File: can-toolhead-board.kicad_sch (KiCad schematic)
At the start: 40 parts, among them J1 MF3-2x2P, J2 USB_C_Receptacle_USB2.0, J3 SH-6P, SW1 SW_Push, SW2 SW_Push, U1 TPS62933, U2 MIC5365-3.3YC5, U3 TJA1051TK-3, U4 STM32G0B1KBU6, U7 USBLC6-2P6

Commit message: Add part number references
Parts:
- C1: MPN EEH-ZK1V101XP -> (none); manf# (none) -> GYE1V101MCQ1GS
- C10, C11, C12, C3, C4, C5: manf# (none) -> GRM155R71H104KE14J
- C2: manf# (none) -> GRM21BR61H106KE43L
- C6: manf# (none) -> CL05C470JB5NNNC
- C7: manf# (none) -> CL10A226MP8NUNE
- C8: manf# (none) -> CL10A475KO8NNNC
- C9: manf# (none) -> CL05B103KB5NNNC
- D1: MPN SS34 -> (none); digikey# (none) -> 641-2115-1-ND; manf# (none) -> SS34
- D2: MPN DSS14 -> (none); digikey# (none) -> 1655-DSS14UCT-ND; manf# (none) -> DSS14
- D6: manf# (none) -> LTST-S270KGKT
- H1, H2, JP1, JP5, JP6: now left out of the parts list
- J1: MPN 43045-0400 -> (none); manf# (none) -> 43045-0400
- J2: MPN TYPE-C-31-M-12 -> (none); manf# (none) -> 12402012E212A
- J3: manf# (none) -> SM06B-SRSS-TB
- JP2: manf# (none) -> M22-2010205
- L1: MPN IHLP2020CZER3R3M11 -> (none); manf# (none) -> IHLP2020CZER3R3M11
- R1: manf# (none) -> RMCF0402JT120R
- R2: value 52K3 -> 52K3 1%; manf# (none) -> RMCF0402FT52K3
- R3: value 10K -> 10K 1%; manf# (none) -> RMCF0402FT10K0
- R31, R7: manf# (none) -> RMCF0402FT10K0
- R4: manf# (none) -> RMCF0402JT100K
- R5, R6: manf# (none) -> RMCF0402JT5K10
- SW1, SW2: MPN KMR211GLFS -> (none); manf# (none) -> EVQ-P7A01P
- U1: MPN TPS62933DRLR -> (none); manf# (none) -> TPS62933DRLR
- U2: MPN TLV70033DCKR -> (none); manf# (none) -> TLV70033DCKR
- U3: manf# (none) -> TJA1051TK/3/1J
- U4: MPN STM32G0B1KBU6 -> (none); manf# (none) -> STM32G0B1KBU6
- U7: MPN USBLC6-2P6 -> (none); manf# (none) -> USBLC6-2P6
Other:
- moved on the sheet: C7

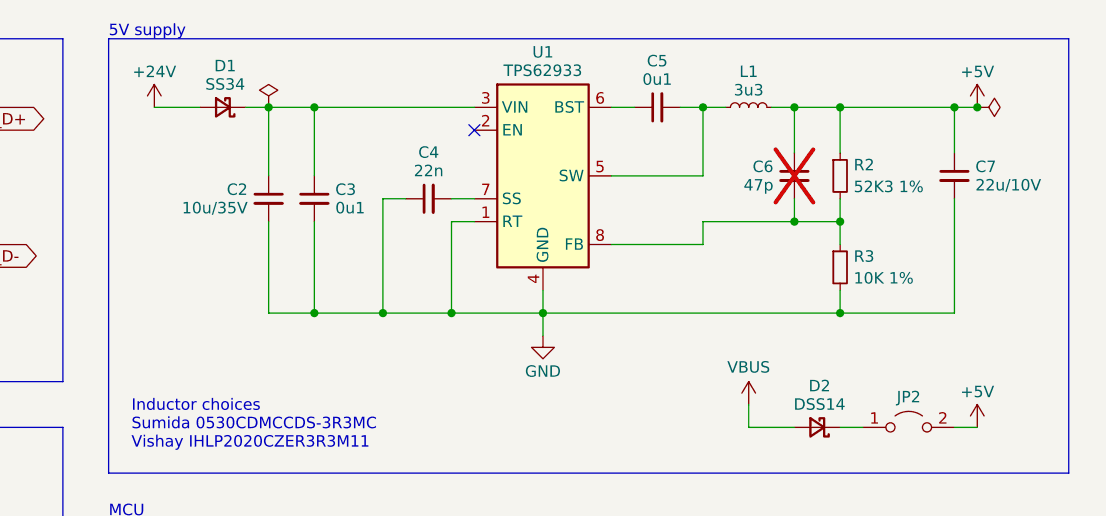
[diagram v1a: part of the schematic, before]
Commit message: Change input caps
- 100uF to electrolytic
- 10uF to 1206/50V
- Also fix LED on BOM to not be right angle lol
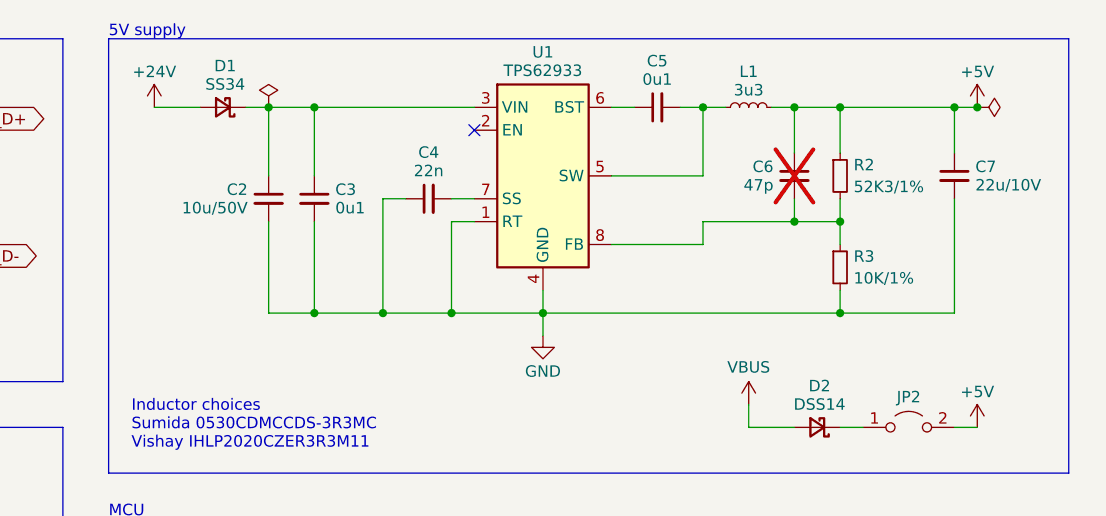
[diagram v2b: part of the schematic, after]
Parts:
- C1: LCSC C454360 -> C705528; manf# GYE1V101MCQ1GS -> EEE-TQV101XAP
- C2: value 10u/35V -> 10u/50V; footprint Capacitor_SMD:C_0805_2012Metric -> Capacitor_SMD:C_1206_3216Metric; LCSC C440198 -> C2987934; manf# GRM21BR61H106KE43L -> GRM31CD71H106KE11
- D6: manf# LTST-S270KGKT -> LTST-C190KGKT
- R2: value 52K3 1% -> 52K3/1%
- R3: value 10K 1% -> 10K/1%
- SW1, SW2: LCSC C221675 -> C79167
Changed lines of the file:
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@@
 			)
 		)
-		(property "Value" "10u/35V"
+		(property "Value" "10u/50V"
 			(at 117.056 41.6703 0)
 			(effects
@@
 			)
 		)
-		(property "Footprint" "Capacitor_SMD:C_0805_2012Metric"
+		(property "Footprint" "Capacitor_SMD:C_1206_3216Metric"
 			(at 119.38 40.64 0)
 			(effects
@@
 			)
 		)
-		(property "manf#" "GRM21BR61H106KE43L"
+		(property "manf#" "GRM31CD71H106KE11 "
 			(at 119.38 40.64 0)
 			(effects
@@
 			)
 		)
-		(property "LCSC" "C440198"
+		(property "LCSC" "C2987934"
 			(at 119.38 40.64 0)
 			(effects
@@
 			)
 		)
-		(property "LCSC" "C221675"
+		(property "LCSC" "C79167"
 			(at 213.36 139.7 0)
 			(effects
@@
 			)
 		)
-		(property "manf#" "LTST-S270KGKT"
+		(property "manf#" "LTST-C190KGKT"
 			(at 261.62 38.1 0)
 			(effects
@@
 			)
 		)
-		(property "LCSC" "C454360"
+		(property "LCSC" "C705528"
 			(at 38.1 39.37 0)
 			(effects
@@
 			)
 		)
-		(property "manf#" "GYE1V101MCQ1GS"
+		(property "manf#" "EEE-TQV101XAP"
 			(at 38.1 39.37 0)
 			(effects
@@
 			)
 		)
-		(property "LCSC" "C221675"
+		(property "LCSC" "C79167"
 			(at 111.76 104.14 0)
 			(effects
@@
 			)
 		)
-		(property "Value" "10K 1%"
+		(property "Value" "10K/1%"
 			(at 184.3786 49.4721 0)
 			(effects
@@
 			)
 		)
-		(property "Value" "52K3 1%"
+		(property "Value" "52K3/1%"
 			(at 184.3786 39.3121 0)
 			(effects

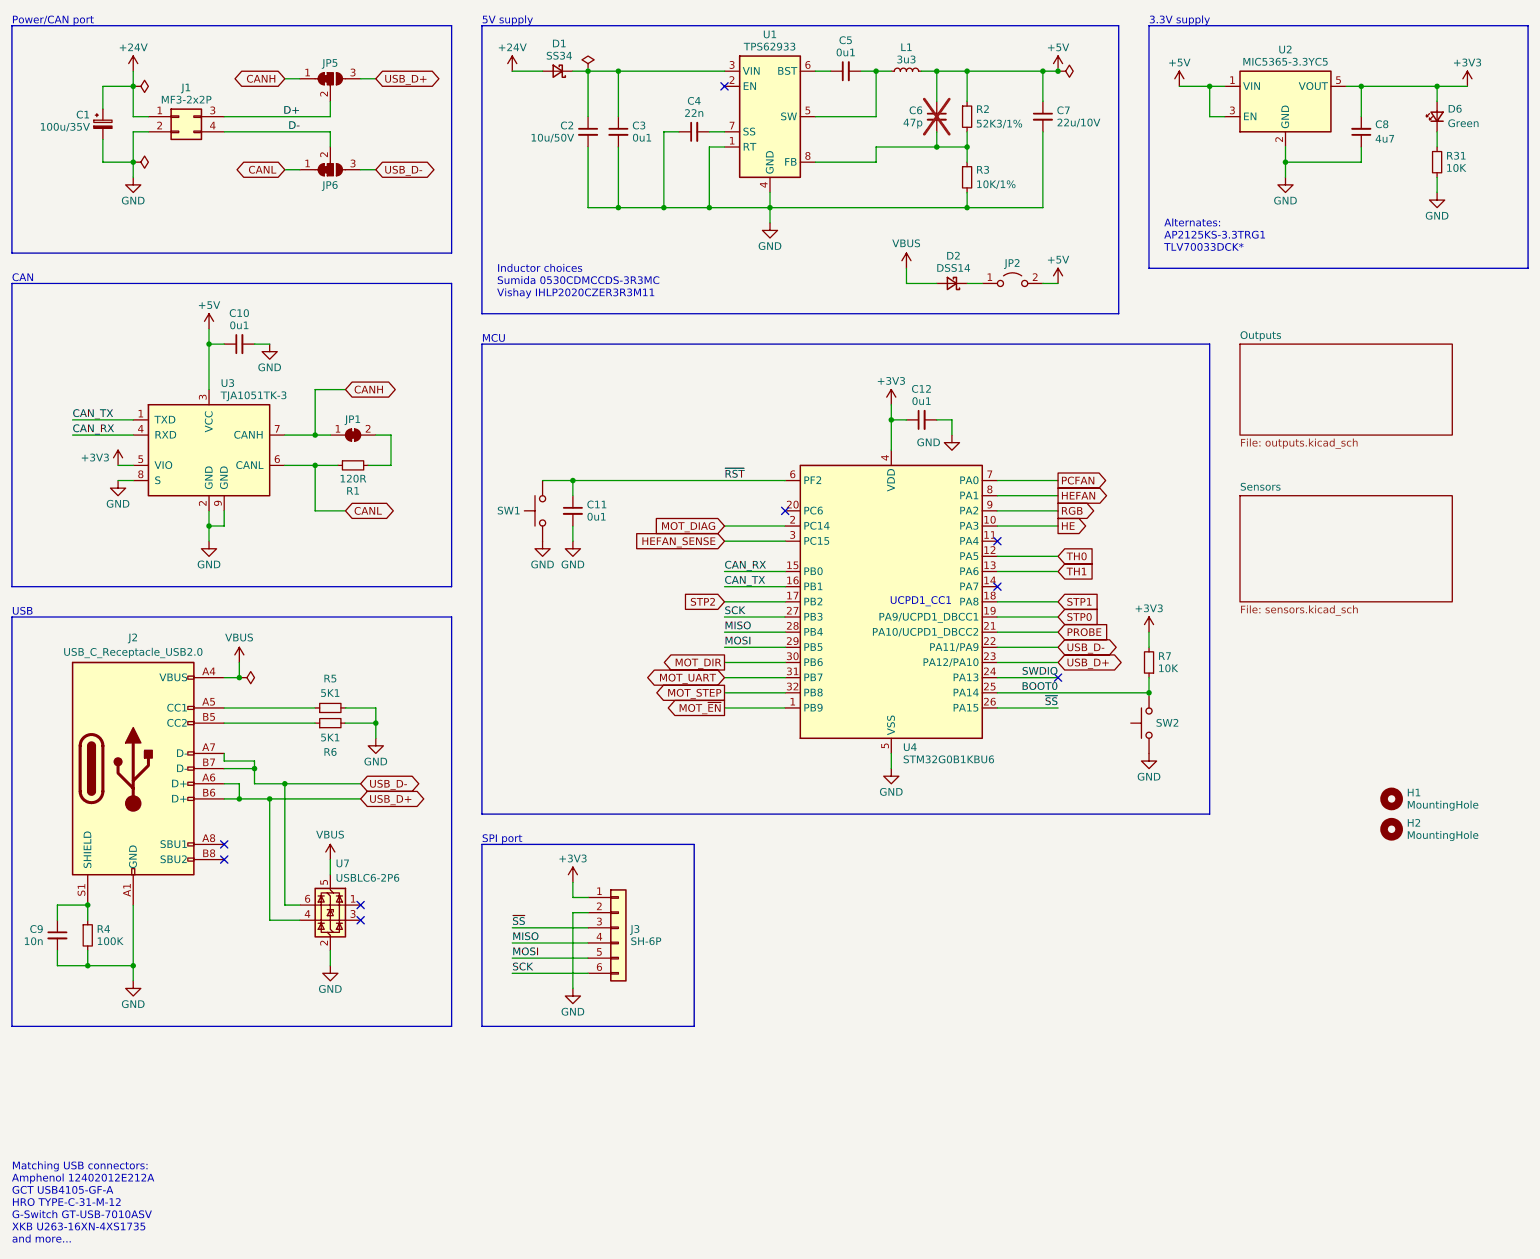
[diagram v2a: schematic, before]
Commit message: Change 5V out cap to 0805
- Shifted power/CAN connector a bit to make room, and added a bit of
  meat to the board around the mounting hole
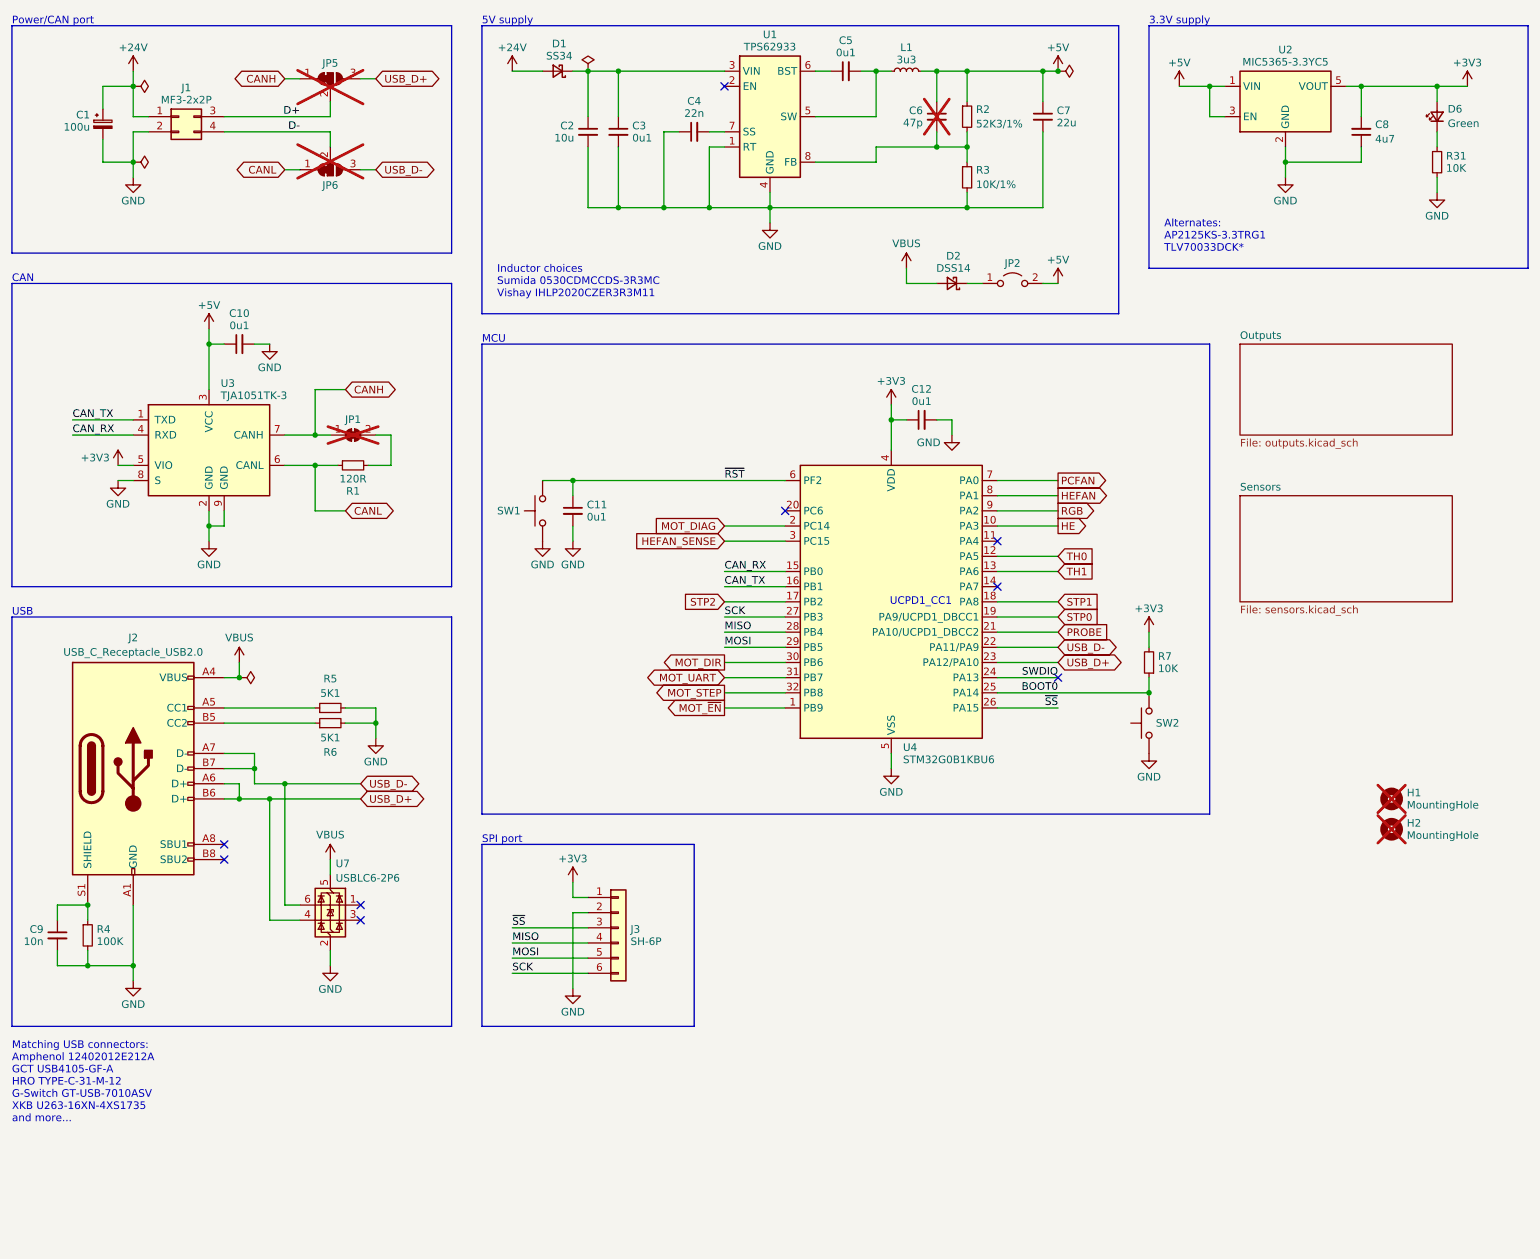
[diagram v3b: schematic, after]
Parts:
- C1: value 100u/35V -> 100u
- C2: value 10u/50V -> 10u; manf# GRM31CD71H106KE11 -> GRM31CD71H106KE11L
- C7: value 22u/10V -> 22u; footprint Capacitor_SMD:C_0603_1608Metric -> Capacitor_SMD:C_0805_2012Metric; LCSC C86295 -> C258782; manf# CL10A226MP8NUNE -> GRM21BC81C226ME44L
- D1: digikey# 641-2115-1-ND -> 4878-SK34SMA-3GCT-ND; mouser# (none) -> 637-SK34SMA-3G
- D2: mouser# (none) -> 241-SS1040FLR100001
- H1, H2, JP1, JP5, JP6: now not fitted
- JP2: manf# M22-2010205 -> NRPN021PAEN-RC;NPN02SXLN-RC
- R1: manf# RMCF0402JT120R -> RC0402FR-07120RL
- R2: digikey# (none) -> YAG3179CT-ND; manf# RMCF0402FT52K3 -> RC0402FR-0752K3L
- R3, R31, R7: manf# RMCF0402FT10K0 -> RC0402FR-0710KL
- R4: manf# RMCF0402JT100K -> RC0402FR-07100KL
- R5, R6: manf# RMCF0402JT5K10 -> RC0402FR-075K1L

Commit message: Update LCSC part numbers
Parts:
- JP2: LCSC C706997 -> C6837593;C5274553
- R2: LCSC C26982 -> C276275
- U3: LCSC C2875699 -> C5382549
- U7: LCSC C15999 -> C2827693
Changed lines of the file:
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@@
 			)
 		)
-		(property "LCSC" "C706997"
+		(property "LCSC" "C6837593;C5274553"
 			(at 190.5 66.04 0)
 			(effects
@@
 			)
 		)
-		(property "LCSC" "C2875699"
+		(property "LCSC" "C5382549"
 			(at 55.88 93.98 0)
 			(effects
@@
 			)
 		)
-		(property "LCSC" "C15999"
+		(property "LCSC" "C2827693"
 			(at 76.2 170.18 0)
 			(effects
@@
 			)
 		)
-		(property "LCSC" "C26982"
+		(property "LCSC" "C276275"
 			(at 182.88 38.1 0)
 			(effects
